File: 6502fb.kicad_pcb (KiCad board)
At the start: 4 copper layers, 140 x 110 mm, 100 parts, among them J1 Conn_01x02, J10 Conn_01x10, J11 Conn_01x03, J12 Conn_01x03, J13 Conn_01x03, J14 Conn_01x03, J15 Conn_01x03, J16 Conn_01x01, J2 Conn_01x08, J3 Conn_01x02, J4 Conn_01x16, J5 Conn_01x02, J6 Conn_01x03, J7 DE15_Receptacle_HighDensity, J8 Conn_01x08, J9 Conn_01x10, U1 74HC86, U10 74AHC30, U11 74AHC30, U12 74AHC30, U13 74AHC30, U14 74LV163, U15 74LV04, U16 74AC109, U17 74LV163, U18 74LV04, U19 74LV08, U2 74HC00, U20 74LV163, U21 74AHC30, U22 74AHC30, U23 74AHC30, U24 74AHC30, U25 74AC109, U26 74LV163, U27 74LV163, U28 74LV163, U29 74HC377, U3 74LV27, U30 74LV32, U31 74LV32, U32 74LV08, U33 74LV08, U4 74HC00, U5 74CBT16390, U6 74CBT16390, U7 AS7C256A-10, U8 AS7C256A-10, U9 74CBT16390, X1 25.175MHz

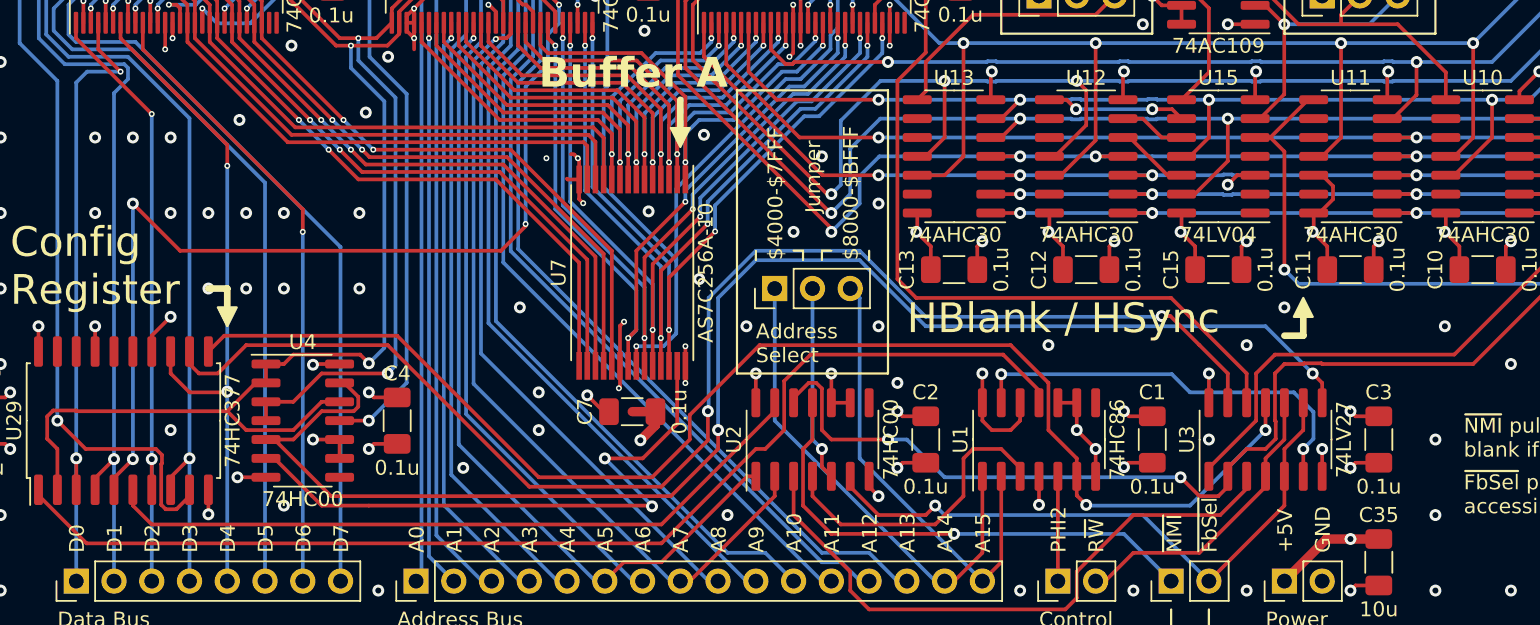
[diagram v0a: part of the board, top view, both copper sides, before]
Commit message: Rename project to 6502fb
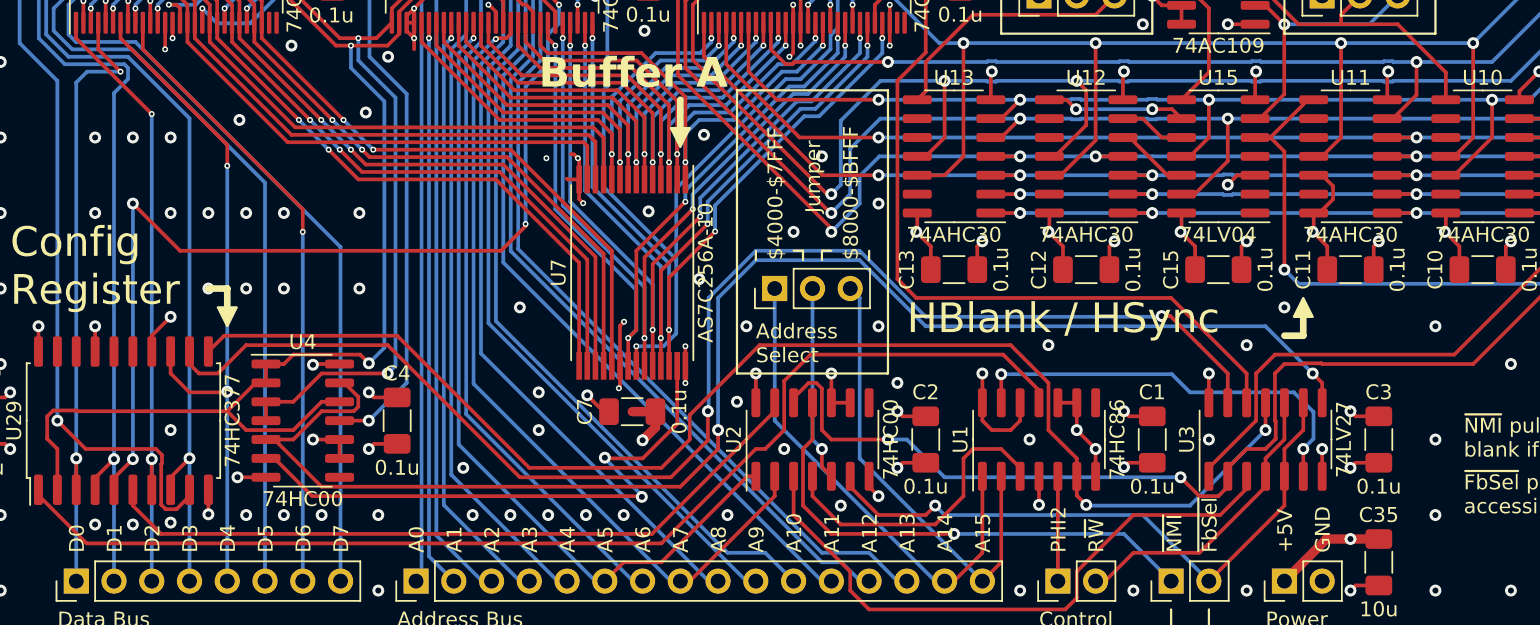
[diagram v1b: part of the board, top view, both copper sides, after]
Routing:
- net /Memory/~{WeA}: track 41.6 -> 39.8 mm
- net /ConfigReg/BlankBlack: track 93.3 -> 92.7 mm
- net /ConfigReg/NmiEnable: track 48.5 -> 49.0 mm
- net /~{Phi2}: track 91.9 -> 91.4 mm
- net /WriteMem: track 99.3 -> 98.8 mm
- net GND: vias 334 -> 349
